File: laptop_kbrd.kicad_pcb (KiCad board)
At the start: 2 copper layers, 141.3 x 42.1 mm, 126 parts, among them CON1 AVR-ISP-6-DR, CON2 AVR-ISP-6-DR, CON3 AVR-ISP-6-DR, K1 CASE_OPEN, K2 CASE_OPEN, Q1 MOSFET_N, Q10 MOSFET_N, Q11 MOSFET_N, Q2 MOSFET_N, Q3 MOSFET_N, Q4 MOSFET_N, Q5 MOSFET_N, Q6 MOSFET_N, Q7 MOSFET_N, Q8 ALS_PT19, Q9 MOSFET_N, SW1 MCU_RST, SW2 BT_ASSCN, SW3 POWER, SW4 CASE_PUSH, SW5 MCU_RST, SW6 MCU_RST, SW7 SPST, U1 ATMEGA32U4-AU, U10 NHD-0440AZ-FL-YBW, U11 NRF24L01+, U12 ATAES132A, U13 AT97SC3205T, U14 TUSB2046BVFR, U15 MAX6749, U16 BME280, U17 TPS2041B, U18 LVDS_HEADER, U2 RT9706, U3 ATMEGA32U4, U4 0WX4JF, U5 XF2M-3015-1A, U6 ATMEGA32U4, U7 USB_CAM, U8 EPAPER_V2, U9 USB_A_FEMALE, X1 XTAL 16MHz, X2 XTAL 16MHz, X3 XTAL 16MHz, X4 6MHz

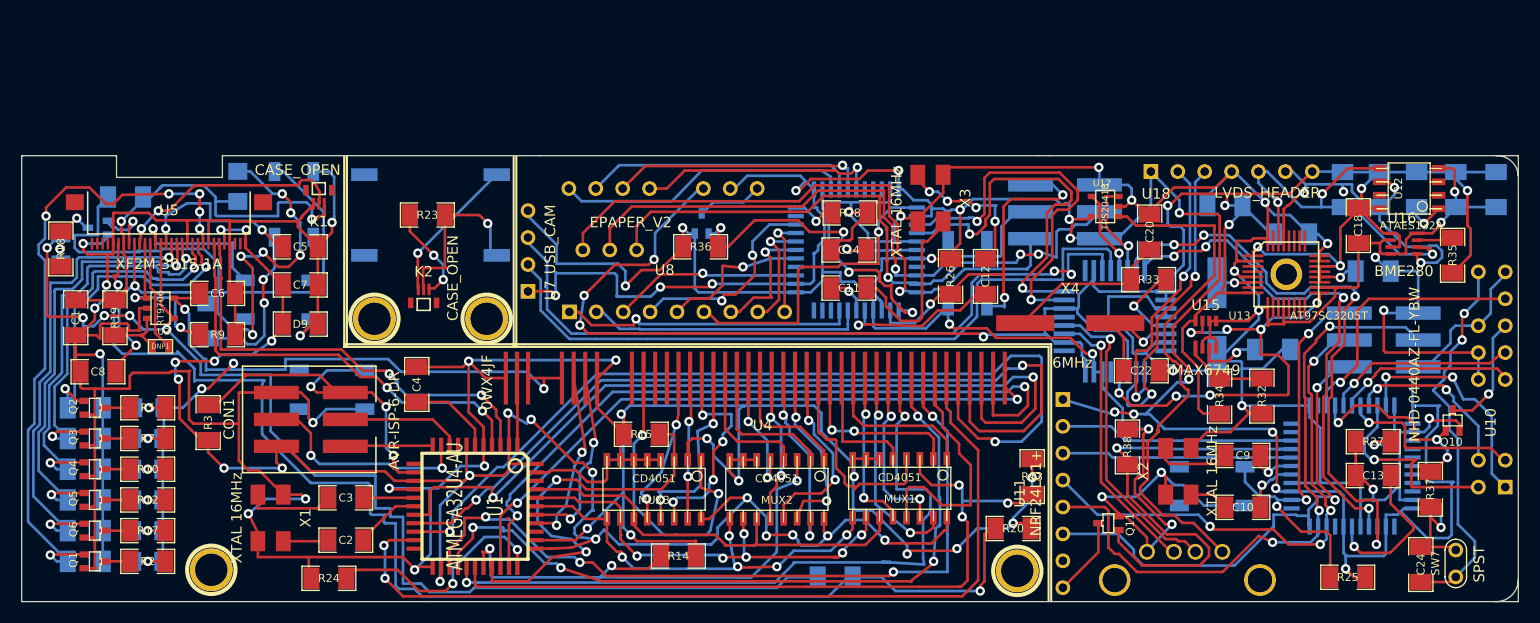
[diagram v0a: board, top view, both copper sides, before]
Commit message: Swapped EPIT1_EPIT0 with GPT_CMPOUT3. Fixed usb d+ d- switch issue.
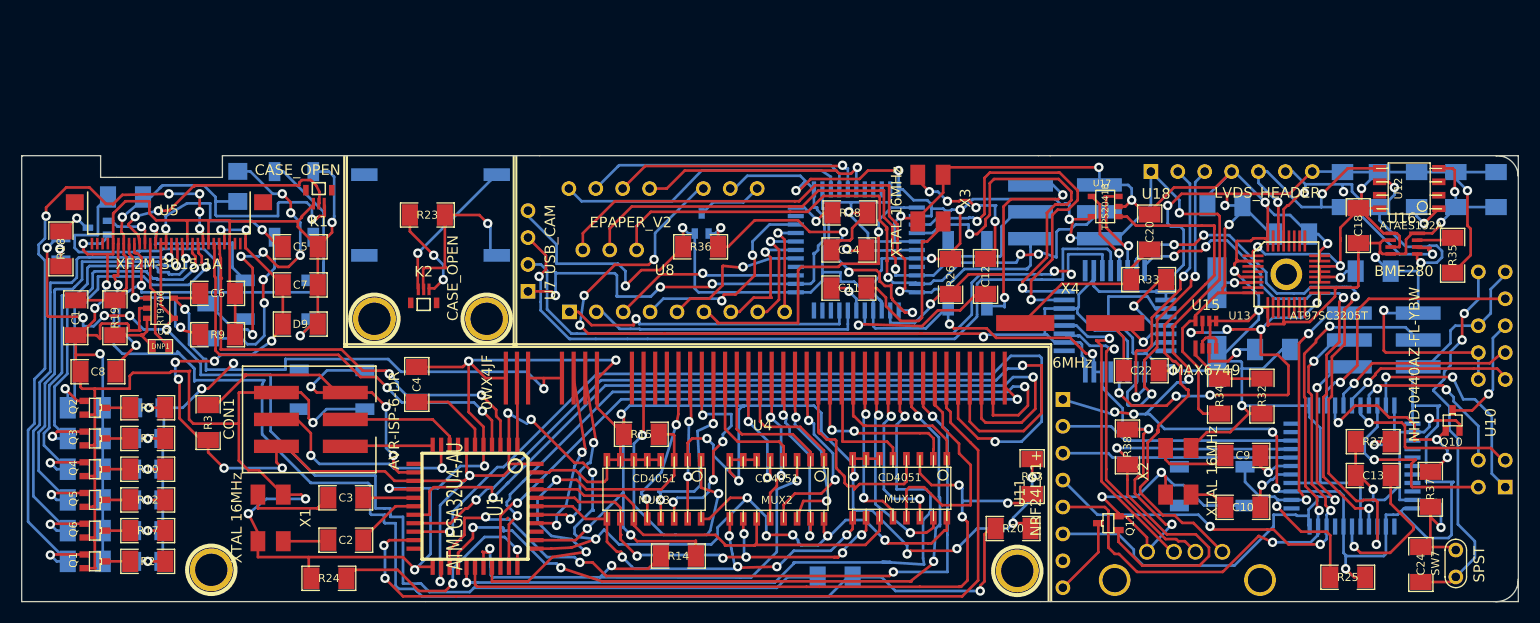
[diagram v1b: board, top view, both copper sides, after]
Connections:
- Q7 pad G: /EPIT1_EPIT0 -> /GPT_CMPOUT3
- R9 pad 1: /GPT_CMPOUT3 -> /EPIT1_EPIT0
- U2 pad 1: /GPT_CMPOUT3 -> /EPIT1_EPIT0
- U7 pad 2: /LCD_board/D3+ -> /LCD_board/D3-
- U7 pad 3: /LCD_board/D3- -> /LCD_board/D3+
- U9 pad 2: /LCD_board/D1+ -> /LCD_board/D1-
- U9 pad 3: /LCD_board/D1- -> /LCD_board/D1+
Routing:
- net /GPT_CMPOUT3: track 15.5 -> 5.12 mm, vias 2 -> 1
- net /EPIT1_EPIT0: track 5.64 -> 15.6 mm, vias 1 -> 2
- net /LCD_board/D3+: track 68.7 -> 72.3 mm, vias 0 -> 1
- net /LCD_board/D1-: track 26.4 -> 29.9 mm
- net /KEY_COL3: track 22.3 -> 23.9 mm
- net /LCD_board/D3-: track 69.3 -> 67.7 mm
- net GND: track 417.5 -> 419.0 mm
- net /KEY_ROW1: track 72.1 -> 72.8 mm
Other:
- outline, holes or cut-outs redrawn

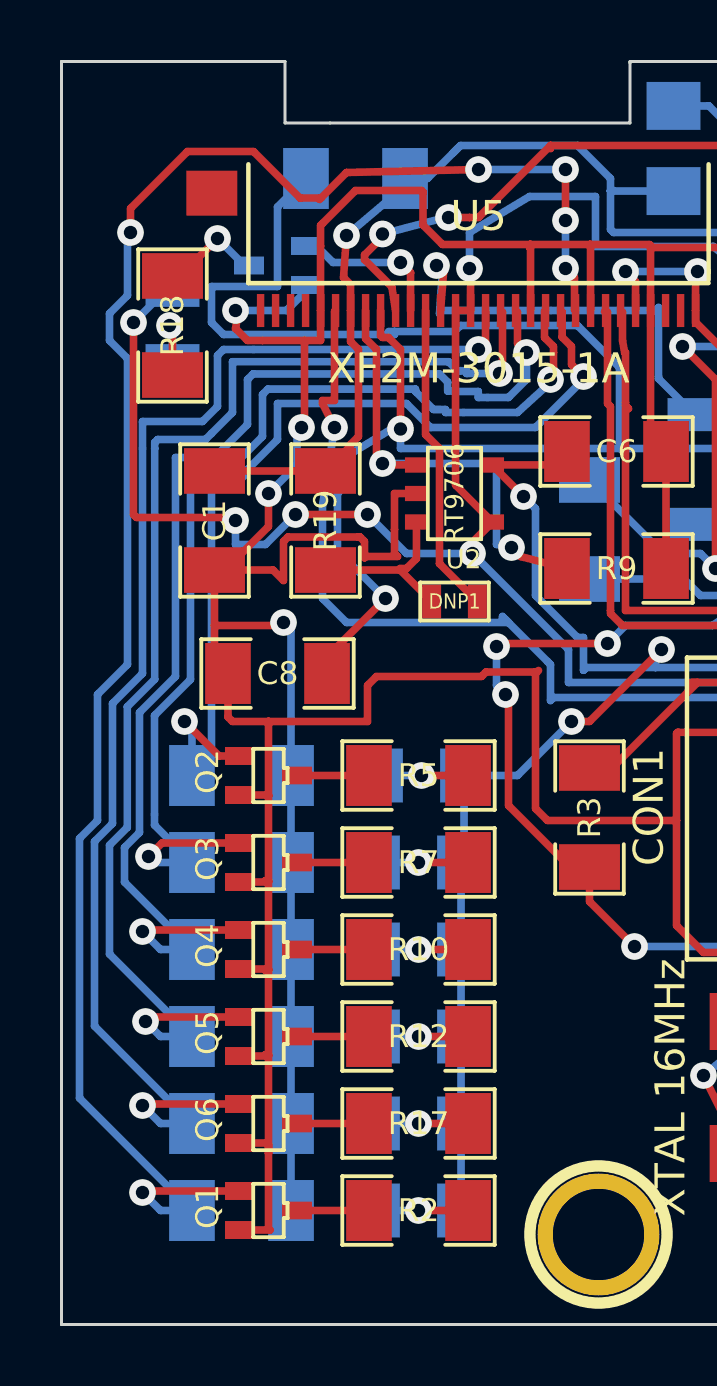
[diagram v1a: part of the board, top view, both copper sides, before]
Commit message: Added 5V breakout to kbrd panel. Changed BOM to reflect proper i2c (vs spi) encrypted eeprom chip. Made gerber files for kbrd only.
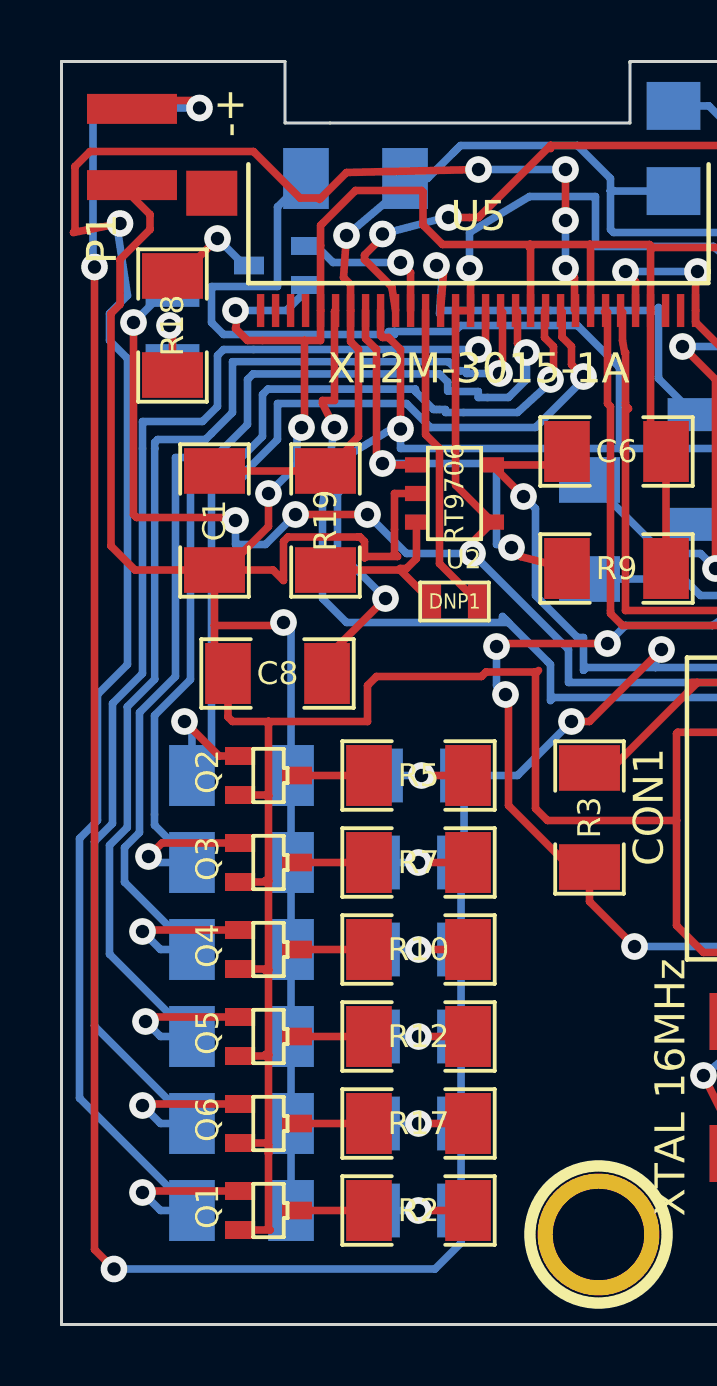
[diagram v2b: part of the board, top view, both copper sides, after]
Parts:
- added P1: -+, 2pin_SMD, F.Cu at (137.4, 122.3)
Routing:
- net VDD: track 72.9 -> 131.0 mm, vias 4 -> 7
- net GND: track 419.0 -> 435.5 mm
- net /FPGA CLK: track 62.5 -> 67.1 mm

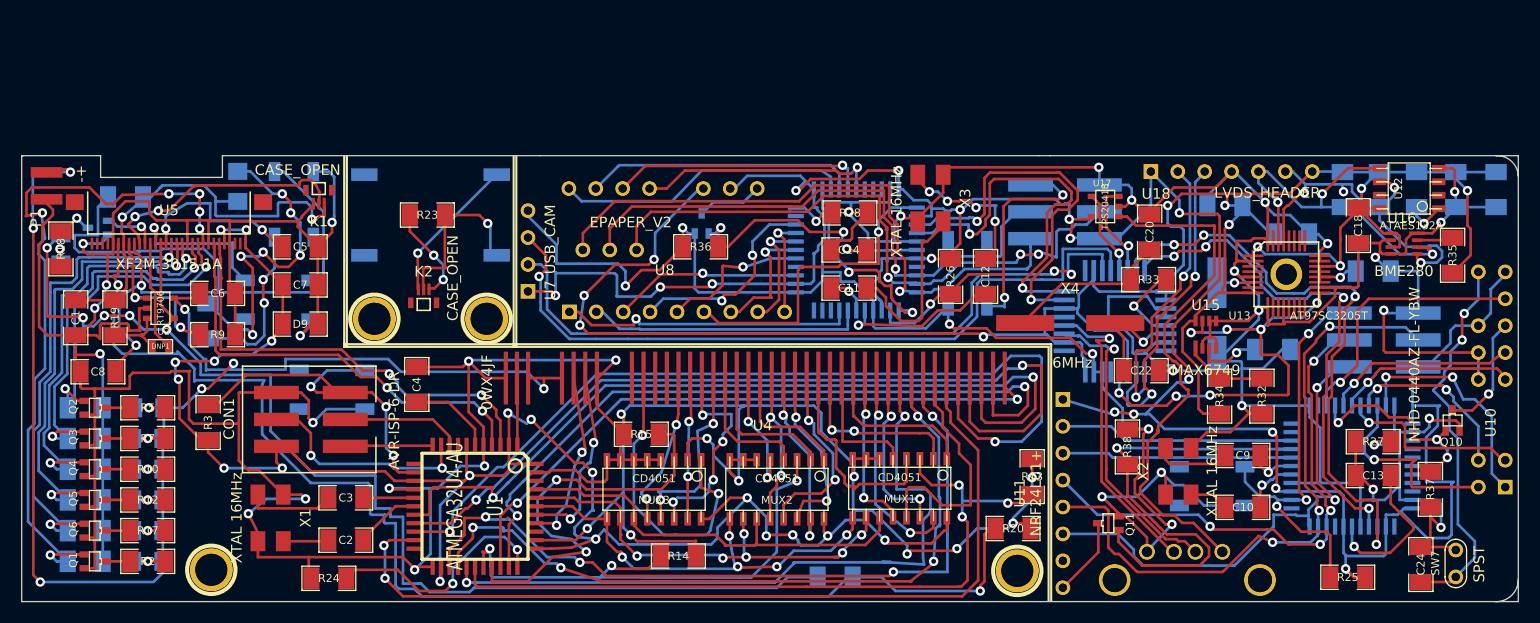
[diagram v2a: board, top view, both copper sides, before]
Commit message: 50 pin FFC cable now goes from motherboard to LCD board.
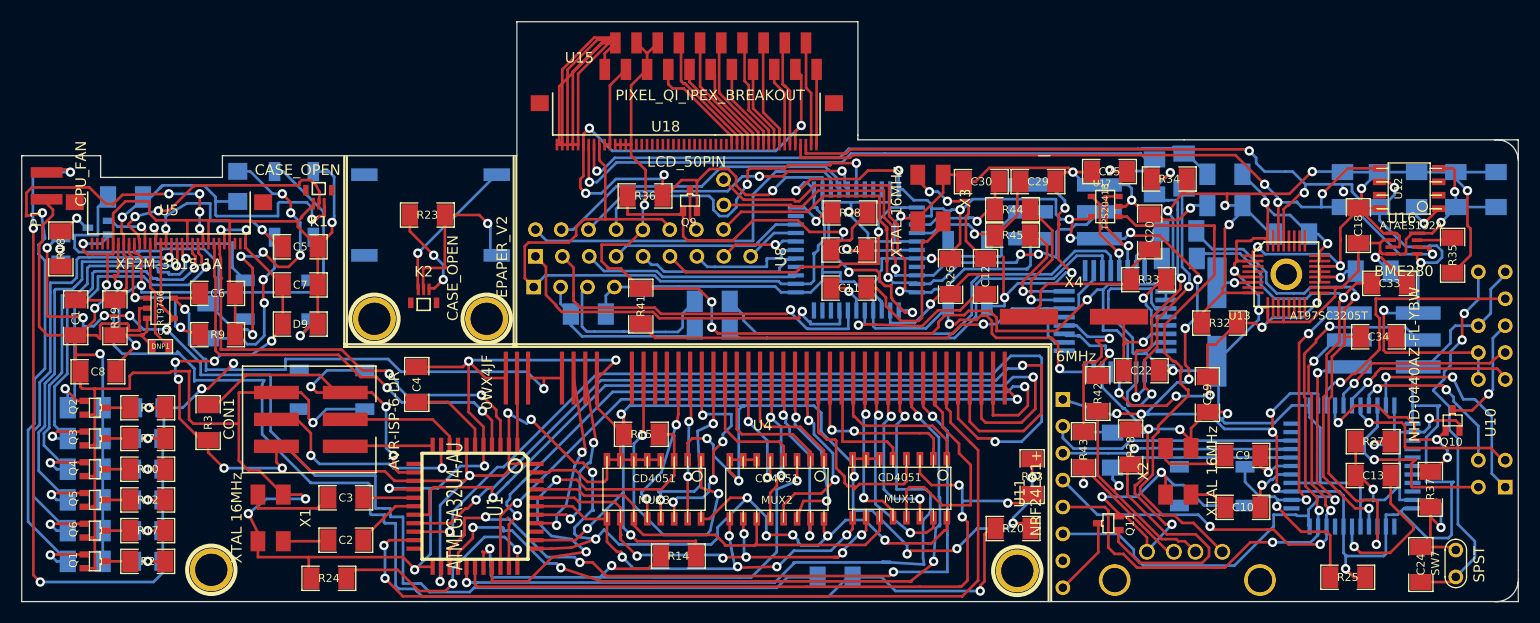
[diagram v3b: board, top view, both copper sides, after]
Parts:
- added C25: 22pF, SM1206, F.Cu at (237.8, 121.0)
- added C26: 22pF, SM1206, B.Cu at (248.7, 121.2)
- added C27: 22pF, SM1206, B.Cu at (235.3, 147.2)
- added C28: 22pF, SM1206, B.Cu at (238.1, 147.2)
- added C29: 22pF, SM1206, F.Cu at (231.0, 121.9)
- added C30: 22pF, SM1206, F.Cu at (225.7, 121.9)
- added C31: 22pF, SM1206, B.Cu at (193.5, 133.7)
- added C32: 22pF, SM1206, B.Cu at (188.6, 134.4)
- added C33: 22pF, SM1206, F.Cu at (264.2, 131.5)
- added C34: 22pF, SM1206, F.Cu at (263.1, 136.6)
- added R39: 27, SM1206, B.Cu at (242.0, 121.5)
- added R40: 27, SM1206, B.Cu at (244.8, 120.9)
- added R41: 10K, SM1206, F.Cu at (193.5, 133.7)
- added R42: 27, SM1206, F.Cu at (236.7, 141.9)
- added R43: 27, SM1206, F.Cu at (235.3, 147.2)
- added R44: 27, SM1206, F.Cu at (228.6, 124.5)
- added R45: 27, SM1206, F.Cu at (228.6, 127.0)
- added R46: 27, SM1206, B.Cu at (244.3, 129.2)
- added R47: 27, SM1206, B.Cu at (244.3, 126.5)
- added R48: 27, SM1206, B.Cu at (200.2, 133.2)
- added R49: 27, SM1206, B.Cu at (200.2, 135.8)
- C19: value 100pF -> 1uF; moved to F.Cu
- P1: value -+ -> CPU_FAN
- Q9: moved to F.Cu
- R32: value 500K -> 15K
- R34: value 500K -> 1.5K
- U15: value MAX6749 -> PIXEL_QI_IPEX_BREAKOUT; footprint SOT23_8 -> Pixel_qi_breakout
- U18: value LVDS_HEADER -> LCD_50PIN; footprint 7pin_0.1inch -> XF2M_5015_1A
- U7: moved to B.Cu
- moved U18 57.8 mm to (192.8, 118.3), turned to 180 degrees
- moved U15 53.0 mm to (200.1, 111.3)
- moved R34 21.0 mm to (243.4, 121.7), turned to 0 degrees
- moved R32 7.98 mm to (248.2, 135.2), turned to 180 degrees
- moved C19 7.48 mm to (247.0, 142.0), turned to 90 degrees
- moved R36 7.11 mm to (193.9, 123.2), turned to 0 degrees
- moved U7 5.52 mm to (187.2, 131.8), turned to 0 degrees
- moved U8 3.06 mm to (192.7, 128.9)
- moved Q9 2.42 mm to (198.2, 123.7), turned to 180 degrees
- moved X4 0.69 mm to (234.4, 134.7)
- moved R38 0.30 mm to (239.8, 146.9)
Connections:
- C19 pad 1: N-00000114 (its old number) -> /LCD_board/GND2
- C19 pad 2: /LCD_board/GND2 -> /LCD_board/~RST
- R32 pad 1: /LCD_board/GND2 -> /LCD_board/~RST
- R32 pad 2: N-00000116 (its old number) -> /LCD_board/V3.32
- R34 pad 1: /LCD_board/V3.32 -> N-00000162
- R34 pad 2: N-00000116 (its old number) -> /LCD_board/V3.32
- U14 pad 1: /LCD_board/Din+ -> N-00000162
- U14 pad 10: /LCD_board/V3.32 -> /LCD_board/OVCR
- U14 pad 11: /LCD_board/D1- -> N-00000158
- U14 pad 12: /LCD_board/D1+ -> N-00000157
- U14 pad 14: /LCD_board/V3.32 -> /LCD_board/OVCR
- U14 pad 15: /LCD_board/D2- -> N-00000156
- U14 pad 16: /LCD_board/D2+ -> N-00000160
- U14 pad 18: /LCD_board/V3.32 -> /LCD_board/OVCR
- U14 pad 19: /LCD_board/D3- -> N-00000152
- U14 pad 2: /LCD_board/Din- -> N-00000164
- U14 pad 20: /LCD_board/D3+ -> N-00000153
- U14 pad 23: /LCD_board/D4- -> N-00000155
- U14 pad 24: /LCD_board/D4+ -> N-00000154
- U14 pad 8: /LCD_board/V3.32 -> /LCD_board/GND2
- U15 pad 1: N-00000116 (its old number) -> N-00000262
- U15 pad 2: /LCD_board/GND2 -> N-00000262
- U15 pad 3: N-00000114 (its old number) -> N-00000196
- U15 pad 4: /LCD_board/GND2 -> /LCD_board/V3.32
- U15 pad 5: /LCD_board/GND2 -> /LCD_board/V3.32
- U15 pad 6: /LCD_board/GND2 -> /LCD_board/V3.32
- U15 pad 7: /LCD_board/~RST -> N-00000182
- U15 pad 8: /LCD_board/V3.32 -> N-00000183
- U18 pad 1: /LCD_board/Vcc2 -> N-00000206
- U18 pad 2: /LCD_board/Din+ -> N-00000191
- U18 pad 3: /LCD_board/Din- -> /LCD_board/SCL
- U18 pad 4: /LCD_board/GND2 -> /LCD_board/SDA
- U18 pad 5: /LCD_board/SDA -> /LCD_board/GND2
- U18 pad 6: /LCD_board/SCL -> N-00000208
- U18 pad 7: /LCD_board/V3.32 -> N-00000207
- U3 pad 24: (no net) -> /LCD_board/Vcc2
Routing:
- net N-00000262: track 0.00 -> 67.4 mm
- net /LCD_board/D3+: track 72.3 -> 17.4 mm, vias 1 -> 0
- net /LCD_board/OVCR: track 0.00 -> 53.1 mm, vias 0 -> 1
- net /LCD_board/D3-: track 67.7 -> 16.4 mm, vias 2 -> 0
- net /LCD_board/SCL: track 34.3 -> 81.8 mm, vias 4 -> 5
- net /LCD_board/GND2: track 444.4 -> 491.0 mm, vias 25 -> 30
- net N-00000153: track 0.00 -> 44.1 mm
- net N-00000152: track 0.00 -> 42.0 mm
- net /LCD_board/SDA: track 36.9 -> 78.7 mm, vias 3 -> 4
- net /LCD_board/Din+: track 27.1 -> 65.5 mm
- net /LCD_board/Din-: track 29.9 -> 62.4 mm, vias 2 -> 1
- net N-00000162: track 0.00 -> 31.6 mm, vias 0 -> 3
- net N-00000164: track 0.00 -> 28.0 mm, vias 0 -> 2
- net /LCD_board/D2-: track 36.1 -> 11.1 mm, vias 2 -> 1
- net /LCD_board/D2+: track 36.2 -> 14.9 mm, vias 2 -> 1
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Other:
- board size 141.3 x 42.1 mm -> 141.3 x 54.8 mm
- board text added: "Rev v1.0a"
